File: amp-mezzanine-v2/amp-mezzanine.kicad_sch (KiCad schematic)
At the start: 11 parts, among them J1 CTRL, J2 PWR, J3 Conn_01x02_MountingPin, J4 Conn_01x02_MountingPin

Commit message: Updated all boards for production
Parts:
- removed A100: R, Jumper:SolderJumper-3_P1.3mm_Open_RoundedPad1.0x1.5mm, symbol Jumper:SolderJumper_3_Open
- removed A101: NC, Jumper:SolderJumper-3_P1.3mm_Open_RoundedPad1.0x1.5mm, symbol Jumper:SolderJumper_3_Open
- removed J2: PWR, Connector_Molex:Molex_PicoBlade_53261-0971_1x09-1MP_P1.25mm_Horizontal, symbol Connector_Generic_MountingPin:Conn_01x09_MountingPin
- added H3, H4: ~, MountingHole:MountingHole_3.2mm_M3_Pad_Via, symbol Mechanical:MountingHole_Pad
- added J2: PWR, Connector_Molex:Molex_PicoBlade_53261-1071_1x10-1MP_P1.25mm_Horizontal, symbol Connector_Generic_MountingPin:Conn_01x10_MountingPin
- H1, H2: value MountingHole_Pad -> ~
- J1: footprint Connector_Molex:Molex_PicoBlade_53261-0971_1x09-1MP_P1.25mm_Horizontal -> Connector_Molex:Molex_PicoBlade_53261-1071_1x10-1MP_P1.25mm_Horizontal; symbol Connector_Generic_MountingPin:Conn_01x09_MountingPin -> Connector_Generic_MountingPin:Conn_01x10_MountingPin
- J3, J4: value Conn_01x02_MountingPin -> ONEWIRE
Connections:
- net +3V3: now also J1.10 (Pin_10); no longer J1.9 (Pin_9)
- net A1: now also J1.2 (Pin_2)
- net CTRL_A: now also J1.8 (Pin_8); no longer J1.7 (Pin_7)
- net CTRL_B: now also J1.7 (Pin_7); no longer J1.6 (Pin_6)
- net CTRL_C: now also J1.6 (Pin_6); no longer J1.5 (Pin_5)
- net CTRL_D: now also J1.5 (Pin_5); no longer J1.4 (Pin_4)
- net EN: now also J1.9 (Pin_9); no longer J1.8 (Pin_8)
- net GND: now also H3.1, H4.1, J2.10 (Pin_10), J2.6 (Pin_6), J2.7 (Pin_7), J2.8 (Pin_8), J2.9 (Pin_9), J2.MP (MountPin)
- net SCL: now also R1.1; no longer R2.1
- net SDA: now also J1.4 (Pin_4), R2.1; no longer J1.2 (Pin_2), R1.1
- net VBUS: now also J2.1 (Pin_1), J2.2 (Pin_2), J2.3 (Pin_3), J2.4 (Pin_4), J2.5 (Pin_5)
- no-connect marks 1 -> 0
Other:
- note added: "CTRL IN NOTE: WIRE HARNESS MUST BE REVERSED (1-10, 2-9, ...)"
- note added: "ONEWIRE OUT NOTE: WIRE HARNESS MUST BE 1-1 FOR DAISY CHAIN"
- note removed: "CTRL IN NOTE: WIRE MUST BE 1-1"
- note removed: "ONEWIRE OUT NOTE: WIRE MUST BE REVERSED TO ALLOW DAISY CHAIN"
- moved on the sheet: R1, R2

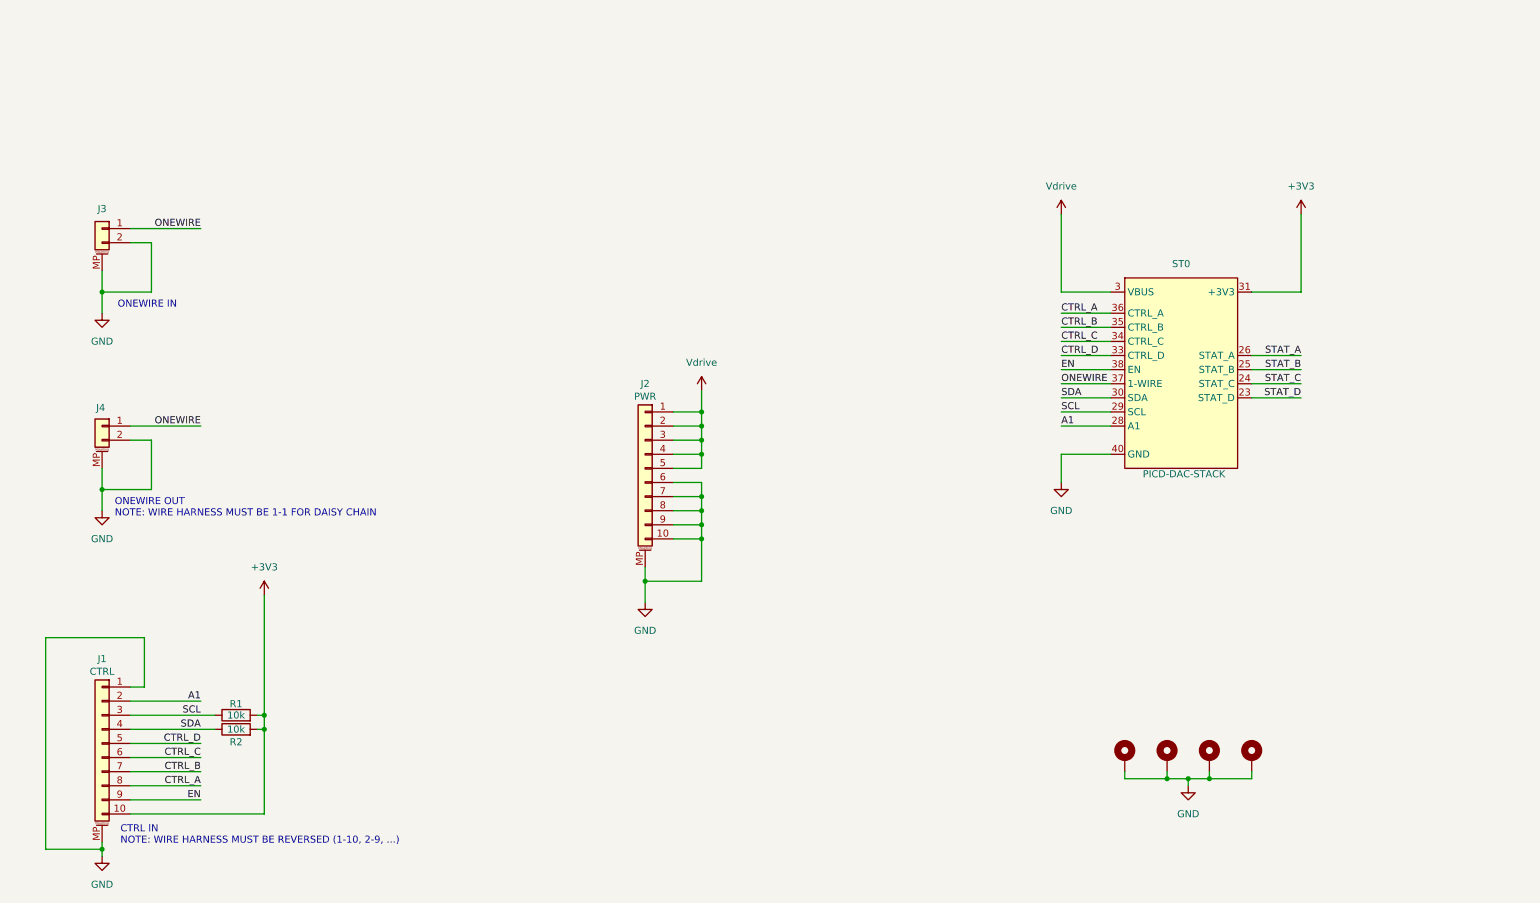
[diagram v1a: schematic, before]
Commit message: Updated mezzanine v2 with Jason & Joe's comments
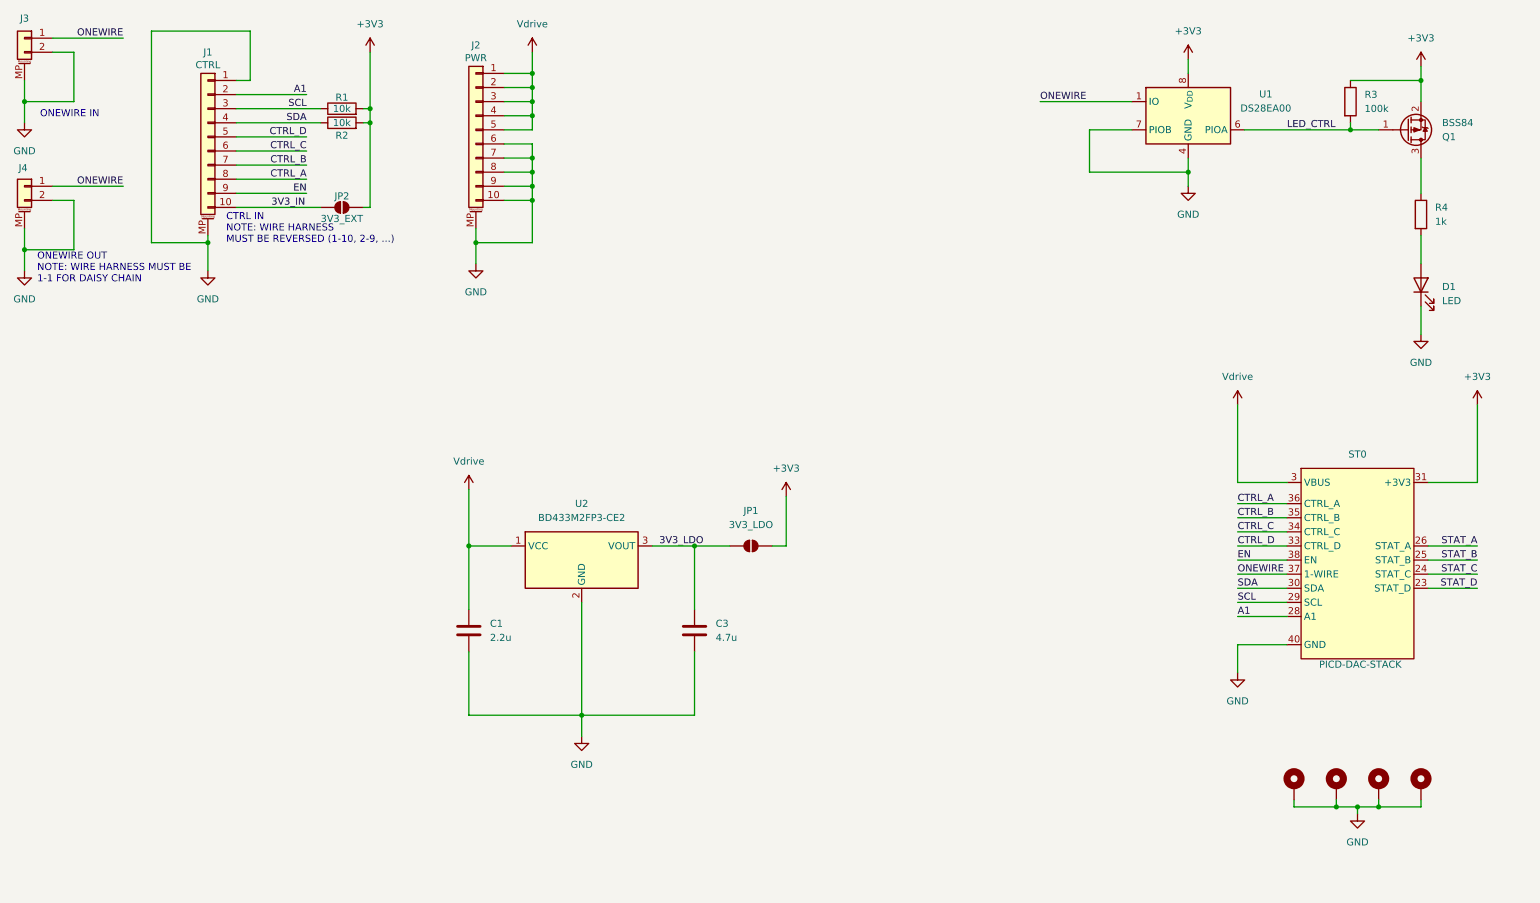
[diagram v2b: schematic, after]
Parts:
- added C1: 2.2u, Capacitor_SMD:C_0805_2012Metric, symbol Device:C
- added C3: 4.7u, Capacitor_SMD:C_0805_2012Metric, symbol Device:C
- added D1: LED, LED_SMD:LED_0402_1005Metric, symbol Device:LED
- added JP1: 3V3_LDO, Jumper:SolderJumper-2_P1.3mm_Open_Pad1.0x1.5mm, symbol Jumper:SolderJumper_2_Open
- added JP2: 3V3_EXT, Jumper:SolderJumper-2_P1.3mm_Open_Pad1.0x1.5mm, symbol Jumper:SolderJumper_2_Open
- added Q1: BSS84, Package_TO_SOT_SMD:SOT-23, symbol Transistor_FET:BSS84
- added R3: 100k, Resistor_SMD:R_0402_1005Metric, symbol Device:R
- added R4: 1k, Resistor_SMD:R_0402_1005Metric, symbol Device:R
- added U1: DS28EA00, Package_SO:MSOP-8_3x3mm_P0.65mm, symbol Sensor_Temperature:DS28EA00
- added U2: BD433M2FP3-CE2, project_footprints:SOT230P700X180-4N, symbol project_symbols:BD433M2FP3-CE2
- J1: footprint Connector_Molex:Molex_PicoBlade_53261-1071_1x10-1MP_P1.25mm_Horizontal -> Connector_Molex:Molex_PicoBlade_53398-1071_1x10-1MP_P1.25mm_Vertical
- J3, J4: footprint Connector_Molex:Molex_PicoBlade_53261-0271_1x02-1MP_P1.25mm_Horizontal -> Connector_Molex:Molex_PicoBlade_53398-0271_1x02-1MP_P1.25mm_Vertical
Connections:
- net +3V3: now also JP1.2 (B), JP2.2 (B), Q1.2 (S), R3.1, U1.8 (V_{DD}); no longer J1.10 (Pin_10)
- net GND: now also C1.2, C3.2, D1.1 (K), U1.4 (GND), U1.7 (PIOB), U2.2 (GND), U2.4 (GND)
- net ONEWIRE: now also U1.1 (IO)
- net VBUS: now also C1.1, U2.1 (VCC)
- new net: D1.2 (A), R4.2
- new net: Q1.3 (D), R4.1
- new net 3V3_IN: J1.10 (Pin_10), JP2.1 (A)
- new net 3V3_LDO: C3.1, JP1.1 (A), U2.3 (VOUT)
- new net LED_CTRL: Q1.1 (G), R3.2, U1.6 (PIOA)
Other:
- moved on the sheet: J1, J2, J3, J4, R1, R2, ST0

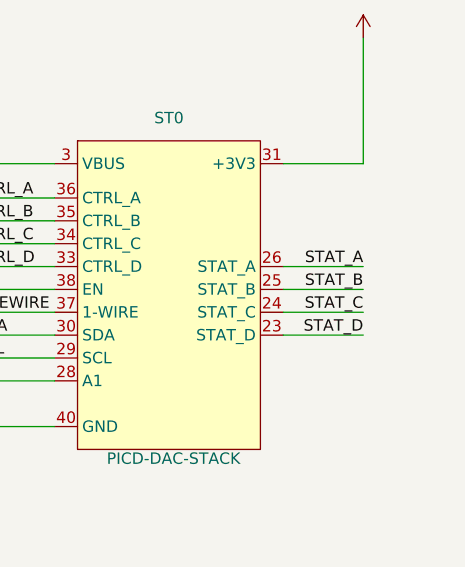
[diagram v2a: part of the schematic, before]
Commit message: Updated amp-mezzanine: added test points
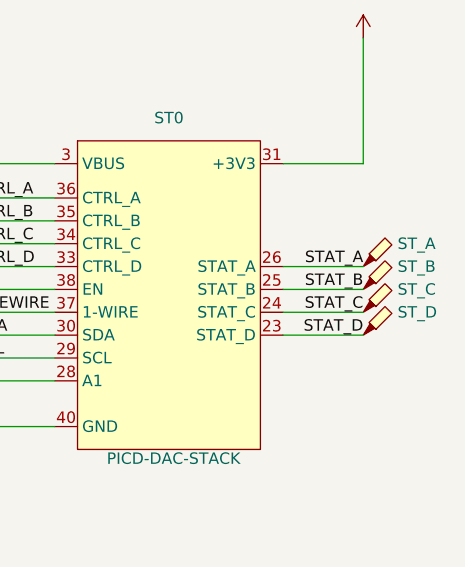
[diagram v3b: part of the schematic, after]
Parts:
- added TP1: ST_A, TestPoint:TestPoint_Pad_D1.0mm, symbol Connector:TestPoint_Probe
- added TP2: ST_B, TestPoint:TestPoint_Pad_D1.0mm, symbol Connector:TestPoint_Probe
- added TP3: ST_C, TestPoint:TestPoint_Pad_D1.0mm, symbol Connector:TestPoint_Probe
- added TP4: ST_D, TestPoint:TestPoint_Pad_D1.0mm, symbol Connector:TestPoint_Probe
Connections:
- net STAT_A: now also TP1.1
- net STAT_B: now also TP2.1
- net STAT_C: now also TP3.1
- net STAT_D: now also TP4.1

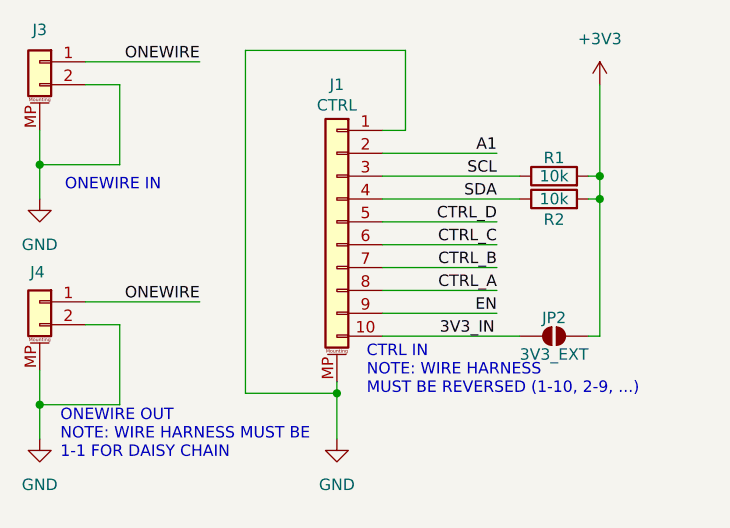
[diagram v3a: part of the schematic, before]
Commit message: Added part numbers
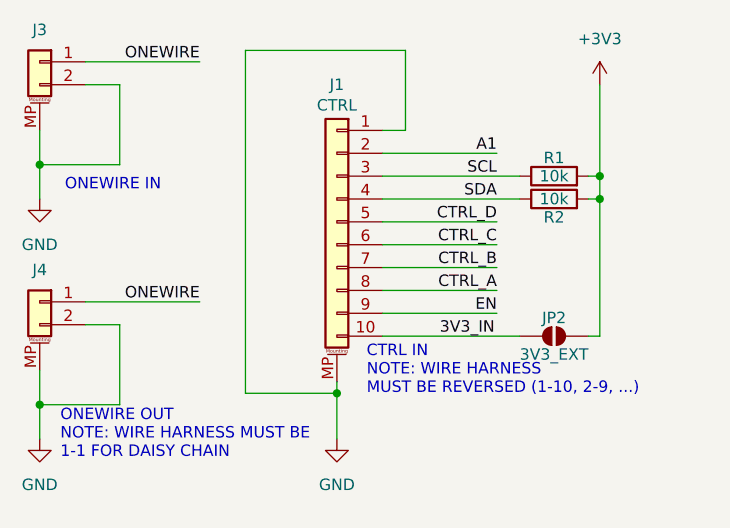
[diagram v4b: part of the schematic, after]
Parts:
- C1: Mfr (none) -> Samsung Electro-Mechanics; Mfr # (none) -> CL21Y225KBYVPNE; Package (none) -> 0805
- C3: Mfr (none) -> TAIYO YUDEN; Mfr # (none) -> MBASE21GBC7475KTCA01; Package (none) -> 0805
- D1: Mfr (none) -> Dialight; Mfr # (none) -> 598-2A00-107F; Package (none) -> 0402
- J1: Mfr (none) -> Molex; Mfr # (none) -> 0533981071; Package (none) -> SMD
- J2: Mfr (none) -> Molex; Mfr # (none) -> 0532611071; Package (none) -> SMD
- J3, J4: Mfr (none) -> Molex; Mfr # (none) -> 0533980271; Package (none) -> SMD
- Q1: Mfr (none) -> onsemi; Mfr # (none) -> BSS84; Package (none) -> SOT-23
- R1, R2: Mfr (none) -> Panasonic; Mfr # (none) -> ERJ-6RBD1002V; Package (none) -> 0805
- R3: Mfr (none) -> Vishay-Dale; Mfr # (none) -> CRCW0402100KFKED; Package (none) -> 0402
- R4: Mfr (none) -> TE Connectivity / Holsworthy; Mfr # (none) -> RP73PF1E1K0BTD; Package (none) -> 0402
- ST0: Mfr (none) -> Amphenol ICC (FCI); Mfr # (none) -> 10132797-045100LF; Package (none) -> SMD
- U1: Mfr (none) -> Analog Devices Inc./Maxim Integrated; Mfr # (none) -> DS28EA00U+; Package (none) -> SMD
- U2: Package (none) -> SMD
